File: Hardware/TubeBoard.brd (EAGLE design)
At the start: 71.1 x 59.3 mm, 20 parts, among them IC1 HV5530PQFP-44

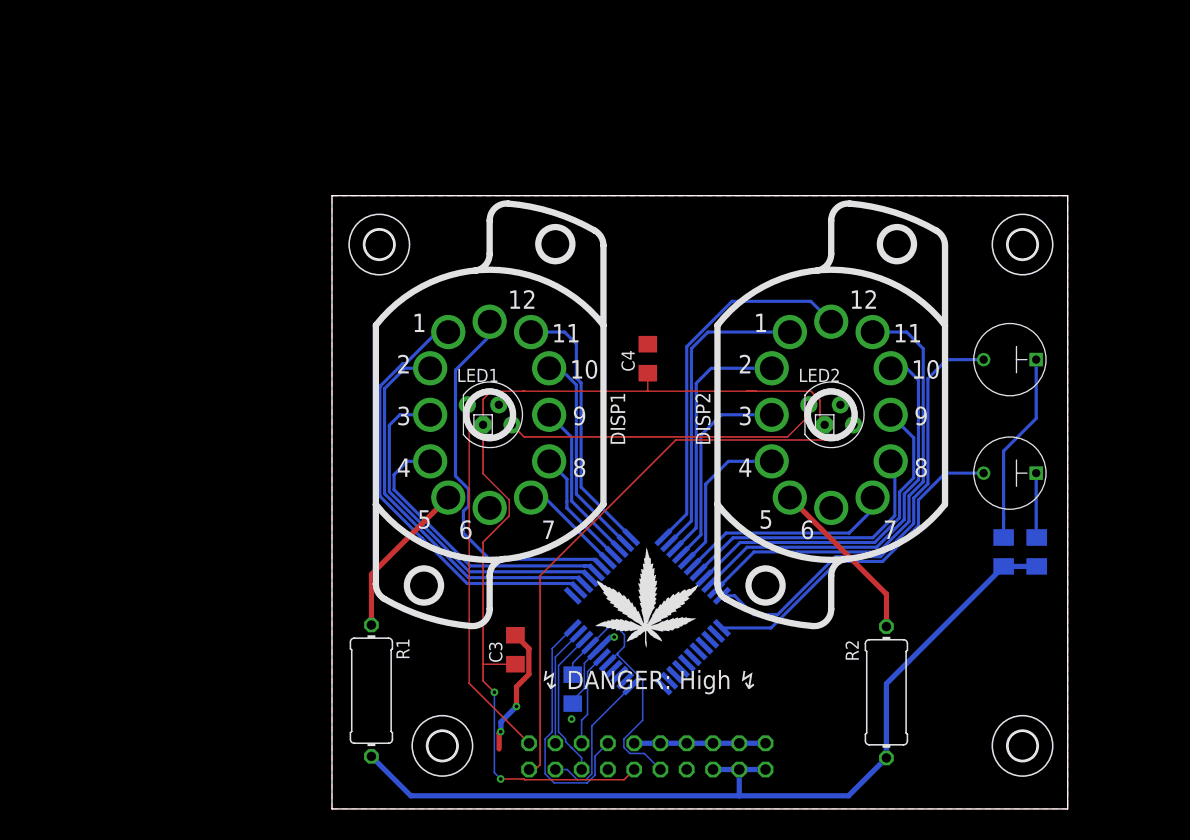
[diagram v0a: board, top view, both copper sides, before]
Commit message: finished tube board schematic
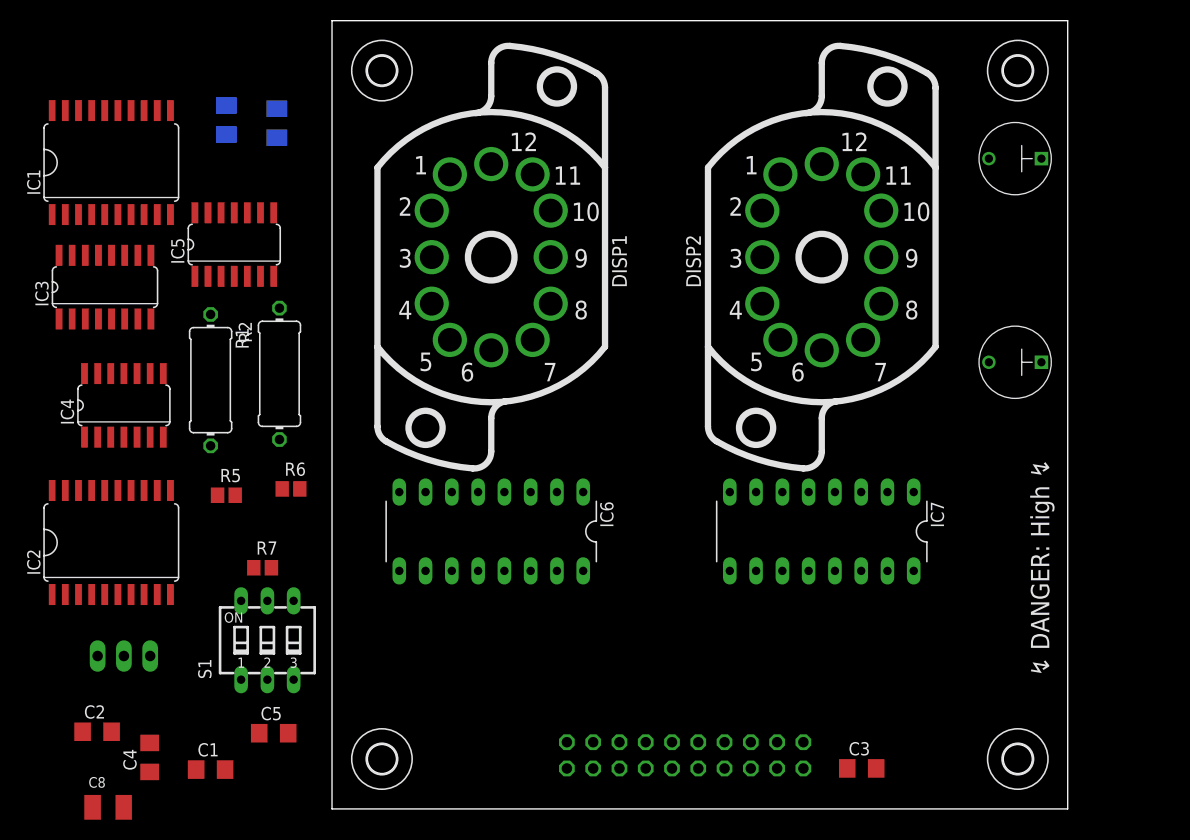
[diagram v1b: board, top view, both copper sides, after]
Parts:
- removed LED1, LED2: (no value), Parts:LED5MMRGB
- removed WEED1: WEED, Parts:DOINK
- added C2, C5: 100nF, rcl:C1206
- added C8: 10µF, rcl:SMC_B
- added IC2: 74HC373DW, 74xx-eu:SO20W
- added IC3: 74HC85D, 74xx-eu:SO16
- added IC4: 74HC04D, 74xx-eu:SO14
- added IC5: 74HC08D, 74xx-eu:SO14
- added IC6, IC7: (no value), Parts:DIL16
- added R5, R6, R7: 10k, rcl:R2012
- added S1: (no value), switch-dil:SD4-03
- added SV2: (no value), con-lstb:MA10-2
- IC1: value HV5530PQFP-44 -> 74HC373DW; device Parts:PQFP44 -> 74xx-eu:SO20W
- SV1: device con-lstb:MA10-2 -> con-lstb:MA03-1
- moved R3 86.0 mm to (-10.2, 66.6)
- moved R4 84.3 mm to (-5.33, 66.3)
- moved IC1 67.6 mm to (-21.3, 62.5), flipped to the top, turned to 0 degrees
- moved R2 66.3 mm to (-5.08, 42.1)
- moved C4 61.7 mm to (-17.6, 4.98)
- moved SV1 51.5 mm to (-20.1, 14.8)
- moved C1 35.9 mm to (-11.7, 3.81), flipped to the top, turned to 0 degrees
- moved C3 35.4 mm to (51.2, 3.91), turned to 0 degrees
- moved R1 33.8 mm to (-11.7, 41.5)
- moved U$1 19.4 mm to (66.0, 62.9)
- moved H4 16.8 mm to (66.3, 71.4)
- moved H3 16.8 mm to (4.83, 71.4)
- moved DISP2 15.3 mm to (47.3, 53.3)
- moved DISP1 15.2 mm to (15.4, 53.3)
- moved U$2 10.7 mm to (66.0, 43.2)
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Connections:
- removed net !K_BLANK: IC1.33, SV1.14
- removed net !K_LATCH: IC1.31, SV1.15
- removed net +12V: C1.1, IC1.27, IC1.30, SV1.9
- removed net K_CLK: IC1.28, SV1.16
- removed net K_DIN: IC1.32, SV1.18
- removed net K_DOUT: IC1.23, SV1.17
- removed net LED_BUS: LED1.4, LED2.1
- removed net LED_DIN: LED1.1, SV1.20
- removed net LED_DOUT: LED2.4, SV1.19
- new net !A0: IC4.4, IC5.5
- new net !NIXIE_CS: IC4.1, SV2.17
- new net A0: IC4.3, IC5.2, SV2.3
- new net A1: SV2.5
- new net A2: IC3.10, SV2.7
- new net A3: IC3.12, SV2.9
- new net A4: IC3.13, SV2.11
- new net BOARD_SELECT: IC5.1, IC5.4, IC5.8
- new net CONTROL_LATCH: IC2.11, IC5.3
- new net D0: IC1.3, IC2.3, SV2.8
- new net D1: IC1.4, IC2.4, SV2.6
- new net D2: IC1.7, IC2.7, SV2.4
- new net D3: IC1.8, IC2.8, SV2.10
- new net D4: IC1.13, IC2.13, SV2.12
- new net D5: IC1.14, IC2.14, SV2.14
- new net D6: IC1.17, IC2.17, SV2.16
- new net D7: IC1.18, IC2.18, SV2.18
- new net DIGIT_LATCH: IC1.11, IC5.6
- new net DRIVE_HI: IC2.19
- new net DRIVE_LO: IC2.15
- new net DRIVE_MED: IC2.16
- new net ID0: IC3.9, R7.1, S1.6
- new net ID1: IC3.11, R6.1, S1.5
- new net ID2: IC3.14, R5.1, S1.4
- new net LDIGIT0: IC1.2, IC6.3
- new net LDIGIT1: IC1.5, IC6.6
- new net LDIGIT2: IC1.6, IC6.7
- new net LDIGIT3: IC1.9, IC6.4
- new net NIXIE_CS: IC4.2, IC5.9
- new net RDIGIT0: IC1.12, IC7.3
- new net RDIGIT1: IC1.15, IC7.6
- new net RDIGIT2: IC1.16, IC7.7
- new net RDIGIT3: IC1.19, IC7.4
- new net SELECT_EN: IC3.6, IC5.10
- net +5V: now also C1.1, C2.1, C5.1, C8.+, IC1.20, IC2.20, IC3.16, IC3.3, IC4.14, IC5.14, IC6.5, IC7.5, S1.1, S1.2, S1.3, SV2.19; no longer LED1.2, LED2.2, SV1.11
- net 1_K0: now also IC6.16; no longer IC1.38
- net 1_K1: now also IC6.15; no longer IC1.40
- net 1_K2: now also IC6.8; no longer IC1.41
- net 1_K3: now also IC6.9; no longer IC1.42
- net 1_K4: now also IC6.13; no longer IC1.43
- net 1_K5: now also IC6.14; no longer IC1.44
- net 1_K6: now also IC6.11; no longer IC1.39
- net 1_K7: now also IC6.10; no longer IC1.35
- net 1_K8: now also IC6.1; no longer IC1.36
- net 1_K9: now also IC6.2; no longer IC1.37
- net 2_K0: now also IC7.16; no longer IC1.5
- net 2_K1: now also IC7.15; no longer IC1.6
- net 2_K2: now also IC7.8; no longer IC1.7
- net 2_K3: now also IC7.9; no longer IC1.8
- net 2_K4: now also IC7.13; no longer IC1.9
- net 2_K5: now also IC7.14; no longer IC1.10
- net 2_K6: now also IC7.11; no longer IC1.1
- net 2_K7: now also IC7.10; no longer IC1.2
- net 2_K8: now also IC7.1; no longer IC1.3
- net 2_K9: now also IC7.2; no longer IC1.4
- net COLON_B: now also IC2.2; no longer IC1.12
- net COLON_T: now also IC2.5; no longer IC1.11
- net GND: now also C2.2, C5.2, C8.-, IC1.1, IC1.10, IC2.1, IC2.10, IC3.1, IC3.15, IC3.2, IC3.4, IC3.8, IC4.7, IC5.7, IC6.12, IC7.12, R5.2, R6.2, R7.2, SV1.1, SV1.3, SV2.1, SV2.2, SV2.20; no longer IC1.29, LED1.3, LED2.3, SV1.10, SV1.12, SV1.2, SV1.4, SV1.6, SV1.8
- net HV_ANODE: now also SV1.2; no longer SV1.1, SV1.3, SV1.5
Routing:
- net +5V: track 94.6 -> 0.00 mm, vias 2 -> 0
- net HV_ANODE: track 88.1 -> 0.00 mm
- net LED_DOUT: track 55.9 -> 0.00 mm
- net 2_K5: track 44.2 -> 0.00 mm
- net COLON_T: track 43.7 -> 0.00 mm
- net 1_K7: track 42.6 -> 0.00 mm
- net 1_K8: track 38.6 -> 0.00 mm
- net 2_K4: track 38.6 -> 0.00 mm
- net 1_K6: track 37.3 -> 0.00 mm
- net 2_K6: track 36.0 -> 0.00 mm
- net LED_DIN: track 35.2 -> 0.00 mm
- net GND: track 33.7 -> 0.00 mm, vias 4 -> 0
- net 1_K9: track 33.7 -> 0.00 mm
- net COLON_B: track 32.9 -> 0.00 mm
- net 2_K3: track 32.7 -> 0.00 mm
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- removed copper zone on layer 1, net GND
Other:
- board size 71.1 x 59.3 mm -> 71.1 x 76.2 mm
- board text added: "IN-12A Serial Driver (c) 2019 Tristan Seifert"
- board text removed: "IN-12A Serial Driver (c) 2018 Tristan Seifert"

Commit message: added transistors to drive colons
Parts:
- added R8, R9: 10k, rcl:R2012
- added T1, T2: MPSA42, transistor:TO92-EBC
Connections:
- new net K_COLON_B: T1.C, U$2.C
- new net K_COLON_T: T2.C, U$1.C
- new net N$5: R8.2, T1.B
- new net N$6: R9.2, T2.B
- net COLON_B: now also R8.1; no longer U$2.C
- net COLON_T: now also R9.1; no longer U$1.C
- net GND: now also T1.E, T2.E
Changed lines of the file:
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@@
 <attribute name="SPICEPREFIX" value="C" x="-27.7368" y="6.7056" size="1.778" layer="27" display="off"/>
+</element>
+<element name="T1" library="transistor" library_urn="urn:adsk.eagle:library:402" package="TO92-EBC" package3d_urn="urn:adsk.eagle:package:29915/2" value="MPSA42" x="76.962" y="42.5196" smashed="yes" rot="R180">
+<attribute name="MOUSER" value="833-MPSA42-AP" x="76.962" y="42.5196" size="1.778" layer="27" rot="R180" display="off"/>
+<attribute name="NAME" x="79.502" y="40.7416" size="1.27" layer="25" ratio="10" rot="R180"/>
+</element>
+<element name="T2" library="transistor" library_urn="urn:adsk.eagle:library:402" package="TO92-EBC" package3d_urn="urn:adsk.eagle:package:29915/2" value="MPSA42" x="77.724" y="61.722" smashed="yes" rot="R180">
+<attribute name="MOUSER" value="833-MPSA42-AP" x="77.724" y="61.722" size="1.778" layer="27" rot="R180" display="off"/>
+<attribute name="NAME" x="80.264" y="59.944" size="1.27" layer="25" ratio="10" rot="R180"/>
+</element>
+<element name="R8" library="rcl" library_urn="urn:adsk.eagle:library:334" package="R2012" package3d_urn="urn:adsk.eagle:package:23543/2" value="10k" x="76.6572" y="36.576" smashed="yes">
+<attribute name="MOUSER" value="652-CR0805FX-1002ELF" x="76.6572" y="36.576" size="1.778" layer="27" display="off"/>
+<attribute name="NAME" x="76.0222" y="37.846" size="1.27" layer="25"/>
+<attribute name="SPICEPREFIX" value="R" x="76.6572" y="36.576" size="1.778" layer="27" display="off"/>
+</element>
+<element name="R9" library="rcl" library_urn="urn:adsk.eagle:library:334" package="R2012" package3d_urn="urn:adsk.eagle:package:23543/2" value="10k" x="77.724" y="55.0164" smashed="yes">
+<attribute name="MOUSER" value="652-CR0805FX-1002ELF" x="77.724" y="55.0164" size="1.778" layer="27" display="off"/>
+<attribute name="NAME" x="77.089" y="56.2864" size="1.27" layer="25"/>
+<attribute name="SPICEPREFIX" value="R" x="77.724" y="55.0164" size="1.778" layer="27" display="off"/>
 </element>
 </elements>
@@
 <contactref element="C2" pad="2"/>
 <contactref element="C8" pad="-"/>
+<contactref element="T2" pad="E"/>
+<contactref element="T1" pad="E"/>
 <wire x1="45.5676" y1="6.4516" x2="46.0756" y2="23.0124" width="0" layer="19" extent="1-1"/>
 <wire x1="45.5676" y1="3.9116" x2="45.5676" y2="6.4516" width="0" layer="19" extent="1-1"/>
@@
 <wire x1="-15.621" y1="57.4548" x2="-17.5006" y2="47.371" width="0" layer="19" extent="1-1"/>
 <wire x1="-5.6388" y1="51.4858" x2="-15.621" y2="57.4548" width="0" layer="19" extent="1-1"/>
+<wire x1="79.502" y1="43.7896" x2="-21.3076" y2="7.4676" width="0" layer="19" extent="1-1"/>
+<wire x1="80.264" y1="62.992" x2="79.502" y2="43.7896" width="0" layer="19" extent="1-1"/>
 </signal>
 <signal name="1_K0">
@@
 </signal>
 <signal name="COLON_T">
-<contactref element="U$1" pad="C"/>
 <contactref element="IC2" pad="5"/>
-<wire x1="-21.971" y1="20.7264" x2="63.5" y2="62.865" width="0" layer="19" extent="1-1"/>
+<contactref element="R9" pad="1"/>
+<wire x1="-21.971" y1="20.7264" x2="76.874" y2="55.0164" width="0" layer="19" extent="1-1"/>
 </signal>
 <signal name="COLON_B">
-<contactref element="U$2" pad="C"/>
 <contactref element="IC2" pad="2"/>
-<wire x1="-25.781" y1="20.7264" x2="63.5" y2="43.18" width="0" layer="19" extent="1-1"/>
+<contactref element="R8" pad="1"/>
+<wire x1="-25.781" y1="20.7264" x2="75.8072" y2="36.576" width="0" layer="19" extent="1-1"/>
 </signal>
 <signal name="D0">
@@
 <contactref element="IC2" pad="19"/>
 </signal>
+<signal name="N$5">
+<contactref element="T1" pad="B"/>
+<contactref element="R8" pad="2"/>
+<wire x1="76.962" y1="43.7896" x2="77.5072" y2="36.576" width="0" layer="19" extent="1-1"/>
+</signal>
+<signal name="N$6">
+<contactref element="T2" pad="B"/>
+<contactref element="R9" pad="2"/>
+<wire x1="77.724" y1="62.992" x2="78.574" y2="55.0164" width="0" layer="19" extent="1-1"/>
+</signal>
+<signal name="K_COLON_B">
+<contactref element="U$2" pad="C"/>
+<contactref element="T1" pad="C"/>
+<wire x1="74.422" y1="43.7896" x2="63.5" y2="43.18" width="0" layer="19" extent="1-1"/>
+</signal>
+<signal name="K_COLON_T">
+<contactref element="U$1" pad="C"/>
+<contactref element="T2" pad="C"/>
+<wire x1="75.184" y1="62.992" x2="63.5" y2="62.865" width="0" layer="19" extent="1-1"/>
+</signal>
 </signals>
